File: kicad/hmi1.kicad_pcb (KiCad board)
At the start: 2 copper layers, 13.2 x 9.7 mm, 3 parts, among them SW2 SW_SPST_0, SW3 SW_SPST_0

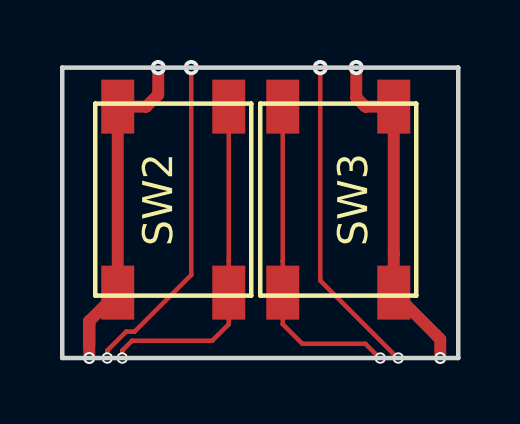
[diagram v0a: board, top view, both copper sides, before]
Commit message: fixed the pb4 issue on the hmi1 side; also cleared drc after fiddling with rules
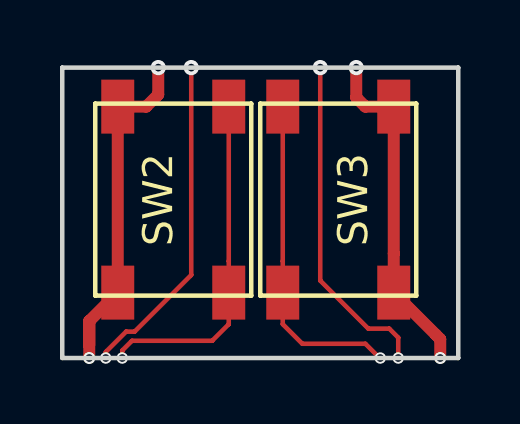
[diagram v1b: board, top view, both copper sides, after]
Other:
- net class Default: via_dia 0.508 -> 0.381
- rule via_min_size: 0.4 -> 0.381
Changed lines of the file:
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@@
     (thickness 1.6)
     (drawings 4)
-    (tracks 46)
+    (tracks 48)
     (zones 0)
     (modules 3)
@@
     (segment_width 0.2)
     (edge_width 0.2)
-    (via_size 0.508)
+    (via_size 0.381)
     (via_drill 0.254)
-    (via_min_size 0.4)
+    (via_min_size 0.381)
     (via_min_drill 0.254)
     (uvia_size 0.3)
@@
     (clearance 0.1524)
     (trace_width 0.127)
-    (via_dia 0.508)
+    (via_dia 0.381)
     (via_drill 0.254)
     (uvia_dia 0.3)
@@
   (segment (start 143.3 92.25) (end 143.3 93.05259) (width 0.4) (layer Top) (net 1))
   (segment (start 143.3 92.25) (end 143.3 93.48) (width 0.4) (layer Top) (net 1))
-  (via (at 143.9 93.48) (size 0.381) (drill 0.254) (layers Top Bottom) (net 2))
-  (segment (start 143.9 93.230593) (end 144.530593 92.6) (width 0.1524) (layer Top) (net 2))
-  (segment (start 143.9 93.5) (end 143.9 93.230593) (width 0.1524) (layer Top) (net 2))
+  (via (at 143.85 93.48) (size 0.381) (drill 0.254) (layers Top Bottom) (net 2))
   (via (at 146.7 83.8) (size 0.508) (drill 0.254) (layers Top Bottom) (net 2))
-  (segment (start 146.7 90.711482) (end 146.7 84) (width 0.1524) (layer Top) (net 2))
-  (segment (start 144.530593 92.6) (end 144.811482 92.6) (width 0.1524) (layer Top) (net 2))
-  (segment (start 144.811482 92.6) (end 146.7 90.711482) (width 0.1524) (layer Top) (net 2))
+  (segment (start 143.85 93.280593) (end 143.85 93.48) (width 0.1524) (layer Top) (net 2))
+  (segment (start 144.530593 92.6) (end 143.85 93.280593) (width 0.1524) (layer Top) (net 2))
+  (segment (start 144.811482 92.6) (end 144.530593 92.6) (width 0.1524) (layer Top) (net 2))
+  (segment (start 146.7 84) (end 146.7 90.711482) (width 0.1524) (layer Top) (net 2))
+  (segment (start 146.7 90.711482) (end 144.811482 92.6) (width 0.1524) (layer Top) (net 2))
   (via (at 144.4 93.48) (size 0.381) (drill 0.254) (layers Top Bottom) (net 3))
   (segment (start 147.95 90.2476) (end 147.95 85.1) (width 0.1524) (layer Top) (net 3))
@@
   (segment (start 150.402411 93.004811) (end 149.75 92.3524) (width 0.1524) (layer Top) (net 4))
   (via (at 153.6 93.48) (size 0.381) (drill 0.254) (layers Top Bottom) (net 5))
-  (segment (start 153.6 93.5) (end 152.8 92.7) (width 0.1524) (layer Top) (net 5))
-  (segment (start 152.8 92.7) (end 151 90.9) (width 0.1524) (layer Top) (net 5))
   (via (at 151 83.8) (size 0.508) (drill 0.254) (layers Top Bottom) (net 5))
   (segment (start 151 90.9) (end 151 84) (width 0.1524) (layer Top) (net 5))
+  (segment (start 152.6 92.5) (end 153.3 92.5) (width 0.1524) (layer Top) (net 5))
+  (segment (start 152.6 92.5) (end 151 90.9) (width 0.1524) (layer Top) (net 5))
+  (segment (start 153.3 92.5) (end 153.6 92.8) (width 0.1524) (layer Top) (net 5))
+  (segment (start 153.6 92.8) (end 153.6 93.48) (width 0.1524) (layer Top) (net 5))
 )
